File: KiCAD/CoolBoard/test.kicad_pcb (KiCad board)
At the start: 2 copper layers, 75 x 90 mm, 15 parts, among them J1 Screw_Terminal_01x02, J2 Screw_Terminal_01x02, J3 Screw_Terminal_01x02, J4 Conn_01x06_Pin, Q1 Q_NMOS_GDS

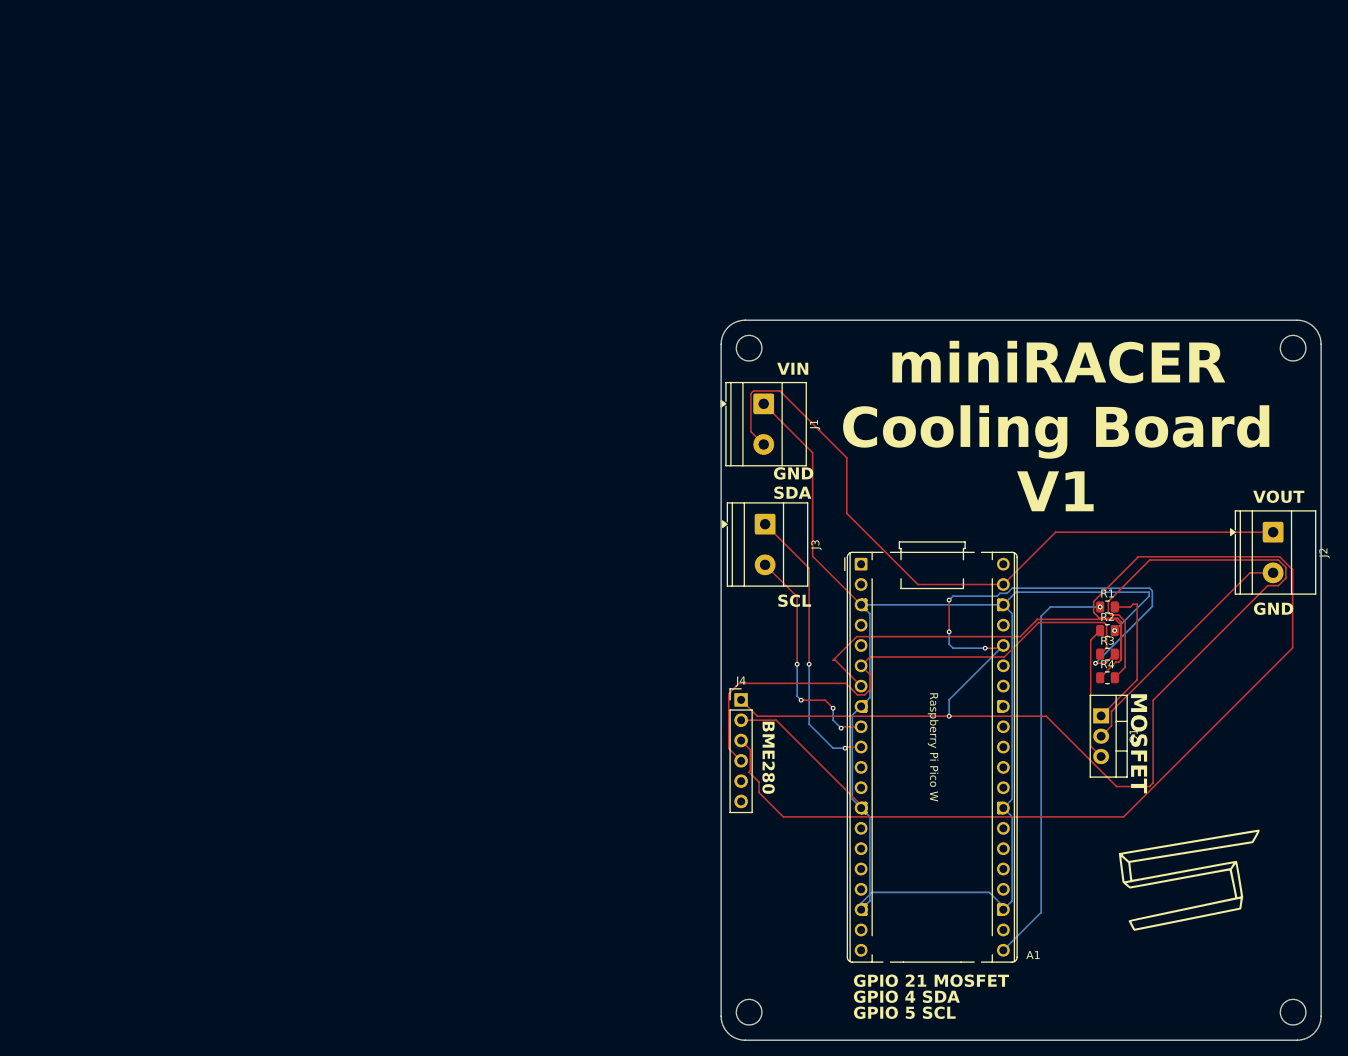
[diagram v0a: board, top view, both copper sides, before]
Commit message: updates to BOM and updates to othere boards (context of kicad pcbs)
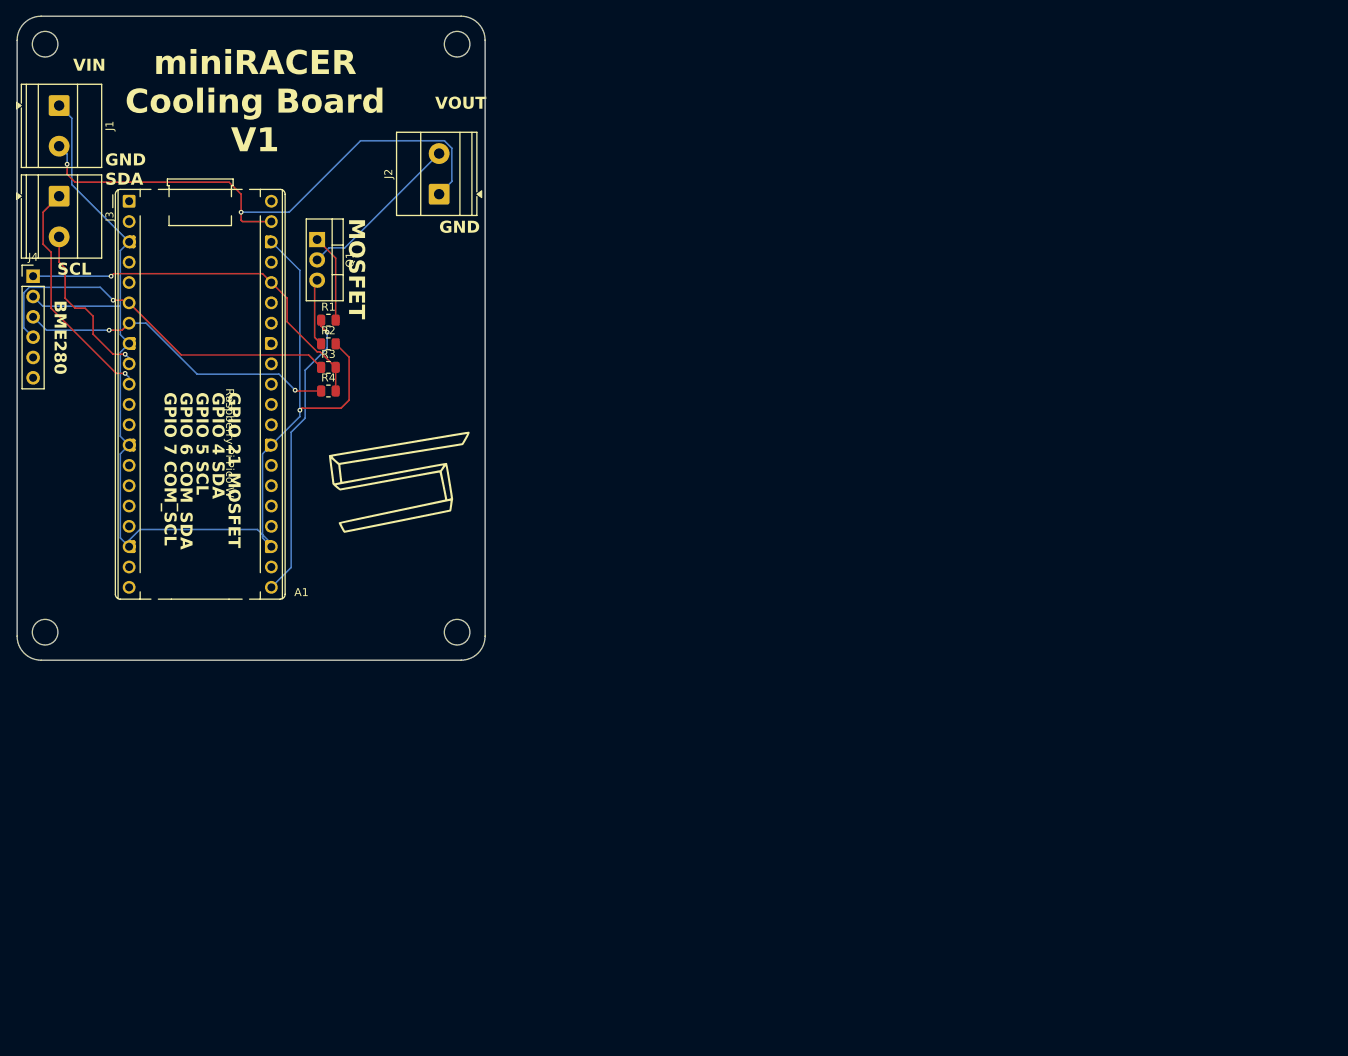
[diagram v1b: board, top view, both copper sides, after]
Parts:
- moved REF** 114.8 mm to (67.0, 89.0)
- moved Q1 114.7 mm to (49.5, 39.9)
- moved J2 112.5 mm to (64.8, 34.2), turned to 90 degrees
- moved REF** 111.2 mm to (67.0, 15.5)
- moved G*** 110.6 mm to (59.8, 70.2)
- moved R1 103.8 mm to (50.9, 50.0)
- moved R2 103.8 mm to (50.9, 53.0)
- moved R3 103.8 mm to (50.9, 55.9)
- moved R4 103.8 mm to (50.9, 58.9)
- moved J4 103.1 mm to (14.0, 44.5)
- moved A1 102.1 mm to (26.0, 35.1)
- moved REF** 100.0 mm to (15.5, 89.0)
- moved J3 97.3 mm to (17.2, 34.5)
- moved REF** 95.9 mm to (15.5, 15.5)
- moved J1 95.6 mm to (17.2, 23.2)
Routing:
- net Net-(A1-3V3): track 192.3 -> 47.5 mm, vias 5 -> 1
- net Net-(A1-GPIO5): track 183.1 -> 40.6 mm, vias 0 -> 3
- net GNDPWR: track 194.2 -> 149.5 mm
- net Net-(A1-GPIO4): track 68.6 -> 47.6 mm, vias 0 -> 2
- net Net-(A1-VSYS): track 89.2 -> 70.6 mm, vias 0 -> 2
- net Net-(A1-GPIO16): track 51.6 -> 36.6 mm
- net Net-(J2-Pin_2): track 31.0 -> 20.8 mm
- net Net-(Q1-S): track 16.8 -> 8.42 mm
- net Net-(Q1-G): track 18.8 -> 11.0 mm
- net Net-(A1-GPIO6): track 28.7 -> 21.1 mm, vias 4 -> 1
- net Net-(A1-GPIO7): track 35.1 -> 29.4 mm, vias 2 -> 1
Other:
- board size 75 x 90 mm -> 58.5 x 80.5 mm
- board text added: "GPIO 6 COM_SDA"
- board text added: "GPIO 7 COM_SCL"
